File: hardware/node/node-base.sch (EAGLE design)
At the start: 43 parts, among them U1 INA322_DGK_8, U2 LMV551_DBV_5, X1 BU-SMA-V

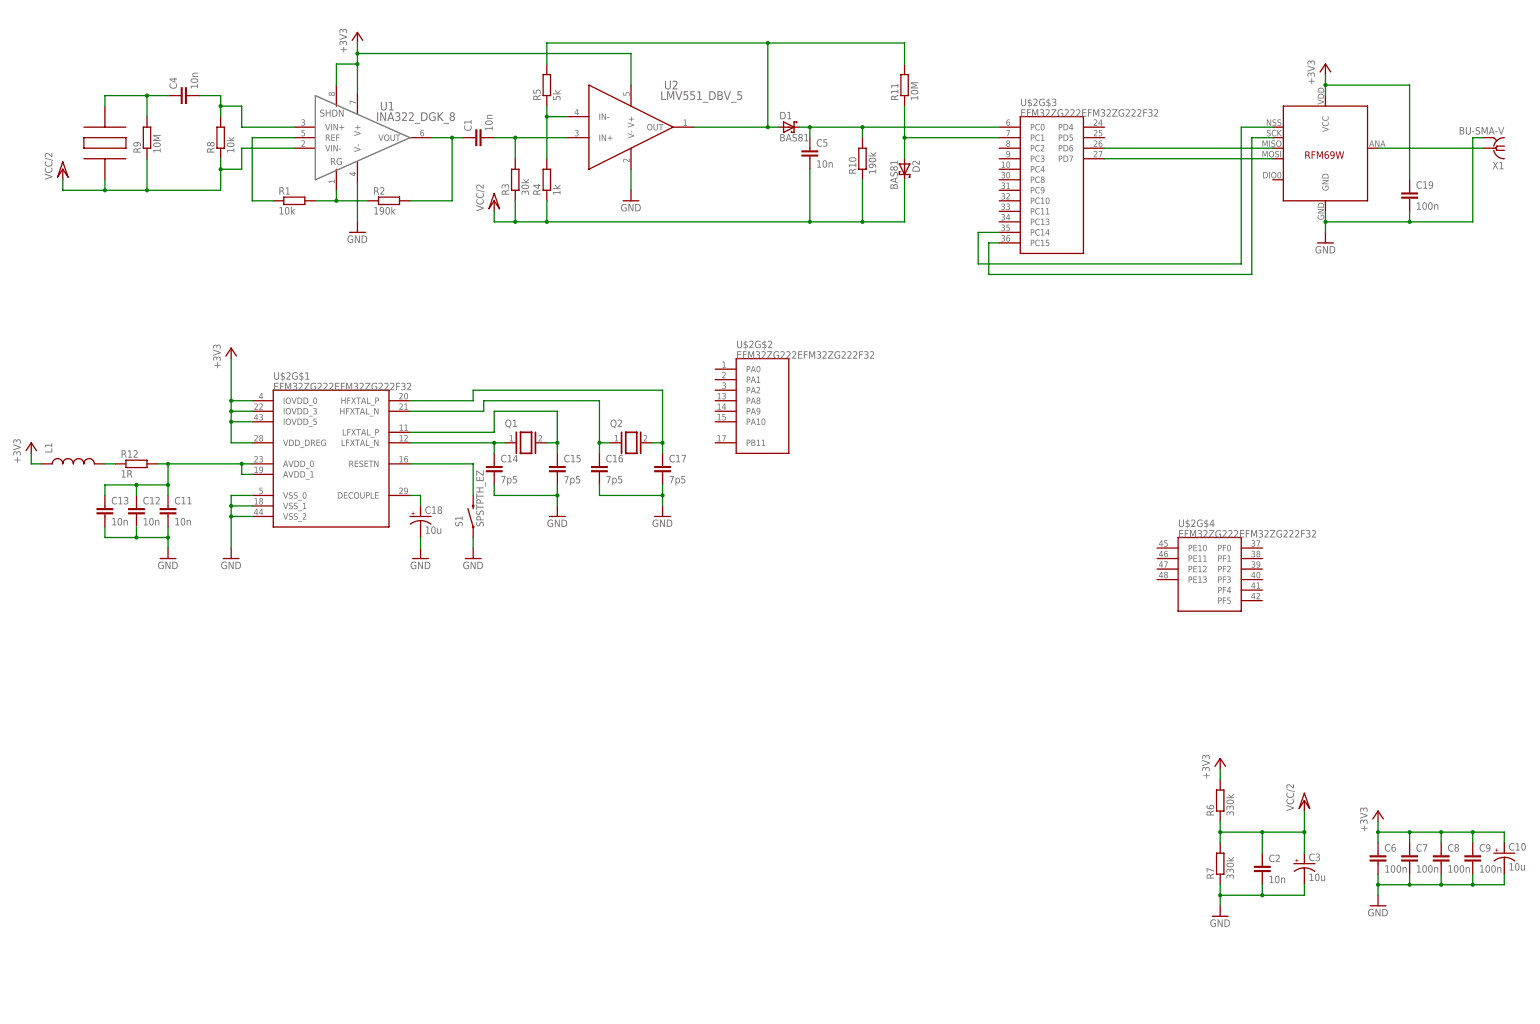
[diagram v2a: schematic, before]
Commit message: NODE: Added sensors, power control
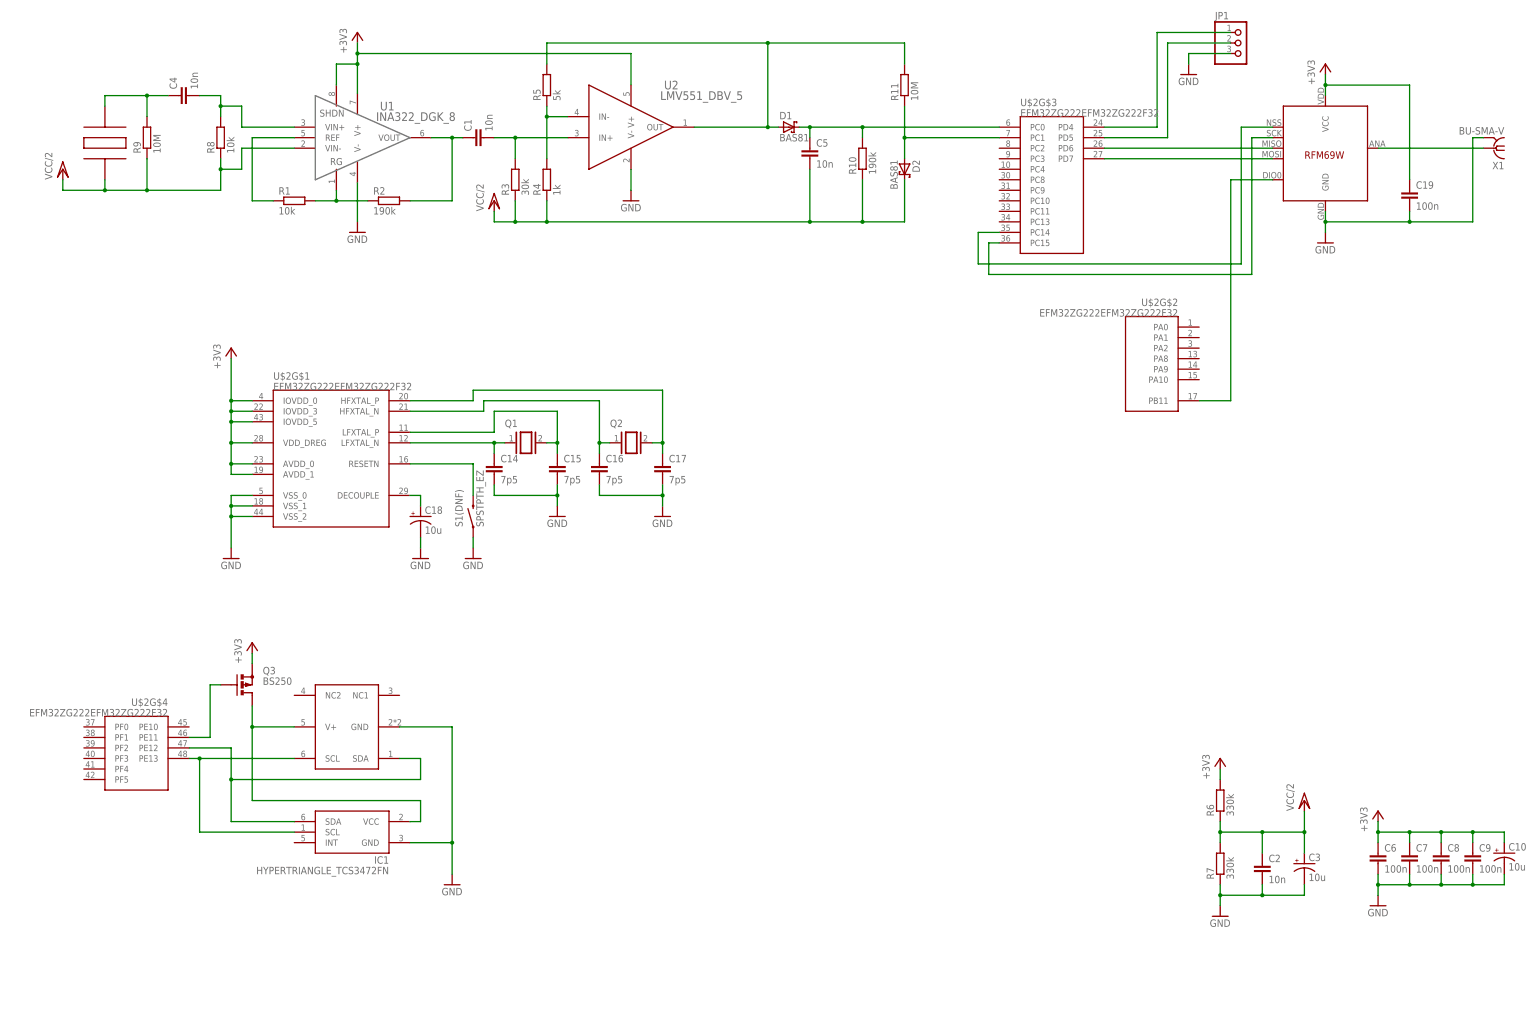
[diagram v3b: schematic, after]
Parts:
- removed C11, C12, C13: 10n, SparkFun-Capacitors:CAPPTH
- removed L1: (no value), SparkFun-Passives:INDUCTOR0805
- removed R12: 1R, resistor:R-EU_0309/12
- added IC1: HYPERTRIANGLE_TCS3472FN, lightsensor:HYPERTRIANGLE_TCS3472FN
- added JP1: (no value), pinhead:PINHD-1X3
- added Q3: BS250, transistor-small-signal:BS250
- added RADIO: RFM69, Moteino:RFM69
- U$3: value RFM69 -> SHT21; device Moteino:RFM69 -> SHT21:SHT21
- renumbered S1 to S1(DNF)
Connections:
- removed net N$6: L1.2, R12.1
- removed net N$8: C11.1, C12.1, C13.1, R12.2, U$2G$1.AVDD_0, U$2G$1.AVDD_1
- new net CON_EXTSENSOR: JP1.1, U$2G$3.PD4
- new net N$21: RADIO.DIO0, U$2G$2.PB11
- new net N$24: IC1.VCC, Q3.D, U$3.V+
- new net N$25: IC1.SCL, U$2G$4.PE13, U$3.SCL
- new net N$26: JP1.2, U$2G$3.PD5
- new net N$27: IC1.SDA, U$2G$4.PE12, U$3.SDA
- new net N$28: Q3.G, U$2G$4.PE11
- net +3V3: now also Q3.S, RADIO.VCC, U$2G$1.AVDD_0, U$2G$1.AVDD_1; no longer L1.1, U$3.VCC
- net GND: now also IC1.GND, JP1.3, RADIO.GND; no longer C11.2, C12.2, C13.2
- net N$13: now also RADIO.MISO; no longer U$3.MISO
- net N$15: now also RADIO.MOSI; no longer U$3.MOSI
- net N$19: now also RADIO.SEL; no longer U$3.SEL
- net N$20: now also RADIO.SCK; no longer U$3.SCK
- net N$22: now also RADIO.ANT; no longer U$3.ANT
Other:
- moved on the sheet: U$2G$2, U$2G$4

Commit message: NODEHW: Finished first schematic draft
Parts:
- added C11: 10n, SparkFun-Capacitors:CAPPTH
- added CON_EXTSENSOR: (no value), pinhead:PINHD-1X3
- added LED1: RED, led:LED3MM
- added LED2: YELLOW, led:LED3MM
- added LED3: GREEN, led:LED3MM
- added R12: 1M, resistor:R-EU_0309/12
- added R13, R14, R15: 220, resistor:R-EU_0309/12
- added S1(DNF)1: SPSTPTH_EZ, SparkFun-Electromechanical:SPSTPTH_EZ
- JP1: device pinhead:PINHD-1X3 -> pinhead:PINHD-1X6
- Q1: value (none) -> 32.768kHz
- Q2: value (none) -> 24MHz
- U$2: value EFM32ZG222EFM32ZG222F32 -> EFM32ZG222F32; device FullyCustom:EFM32ZG222EFM32ZG222F32 -> FullyCustom:EFM32ZG222F32
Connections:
- net N$1 renamed RGLINE
- net N$10 renamed INSTR_FILTERED
- net N$11 renamed OPAMP_VGND
- net N$13 renamed RADIO_MISO
- net N$14 renamed LFXTAL_P
- net N$15 renamed RADIO_MOSI
- net N$16 renamed LFXTAL_N
- net N$17 renamed XTALP
- net N$18 renamed XTALN
- net N$19 renamed RADIO_CS
- net N$2 renamed OPAMP_OUT
- net N$20 renamed RADIO_SCK
- net N$21 renamed RADIO_INT
- net N$22 renamed RADIO_ANT
- net N$23 renamed DECOUPLE
- net N$24 renamed EXT_PWRLINE
- net N$25 renamed SCL
- net N$27 renamed SDA
- net N$28 renamed EXT_PWRUP
- net N$3 renamed DETECT_REF
- net N$4 renamed PIEZO_FILTERED
- net N$5 renamed PIEZO_OUT
- net N$7 renamed REFLINE
- net N$9 renamed INSTR_OUT
- removed net CON_EXTSENSOR: JP1.1, U$2G$3.PD4
- removed net N$12: S1(DNF).2, U$2G$1.RESETN
- removed net N$26: JP1.2, U$2G$3.PD5
- new net EXTSENS_RX: CON_EXTSENSOR.2, U$2G$3.PD5
- new net EXTSENS_TX: CON_EXTSENSOR.1, U$2G$3.PD4
- new net LED_GREEN: LED3.A, U$2G$4.PF3
- new net LED_RED: LED1.A, U$2G$4.PF5
- new net LED_SWITCH: C11.1, R12.1, S1(DNF)1.2, U$2G$4.PE10
- new net LED_YELLOW: LED2.A, U$2G$4.PF4
- new net N$10: LED2.C, R14.2
- new net N$11: LED3.C, R15.2
- new net N$9: LED1.C, R13.2
- new net RESET: JP1.5, S1(DNF).2, U$2G$1.RESETN
- new net SWCLK: JP1.2, U$2G$4.PF0
- new net SWDIO: JP1.4, U$2G$4.PF1
- new net SWO: JP1.6, U$2G$4.PF2
- net +3V3: now also JP1.1, R12.2
- net GND: now also C11.2, CON_EXTSENSOR.3, R13.1, R14.1, R15.1, S1(DNF)1.1
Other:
- note added: "MCU Power & Debug"
- note added: "Sensors & Radio"

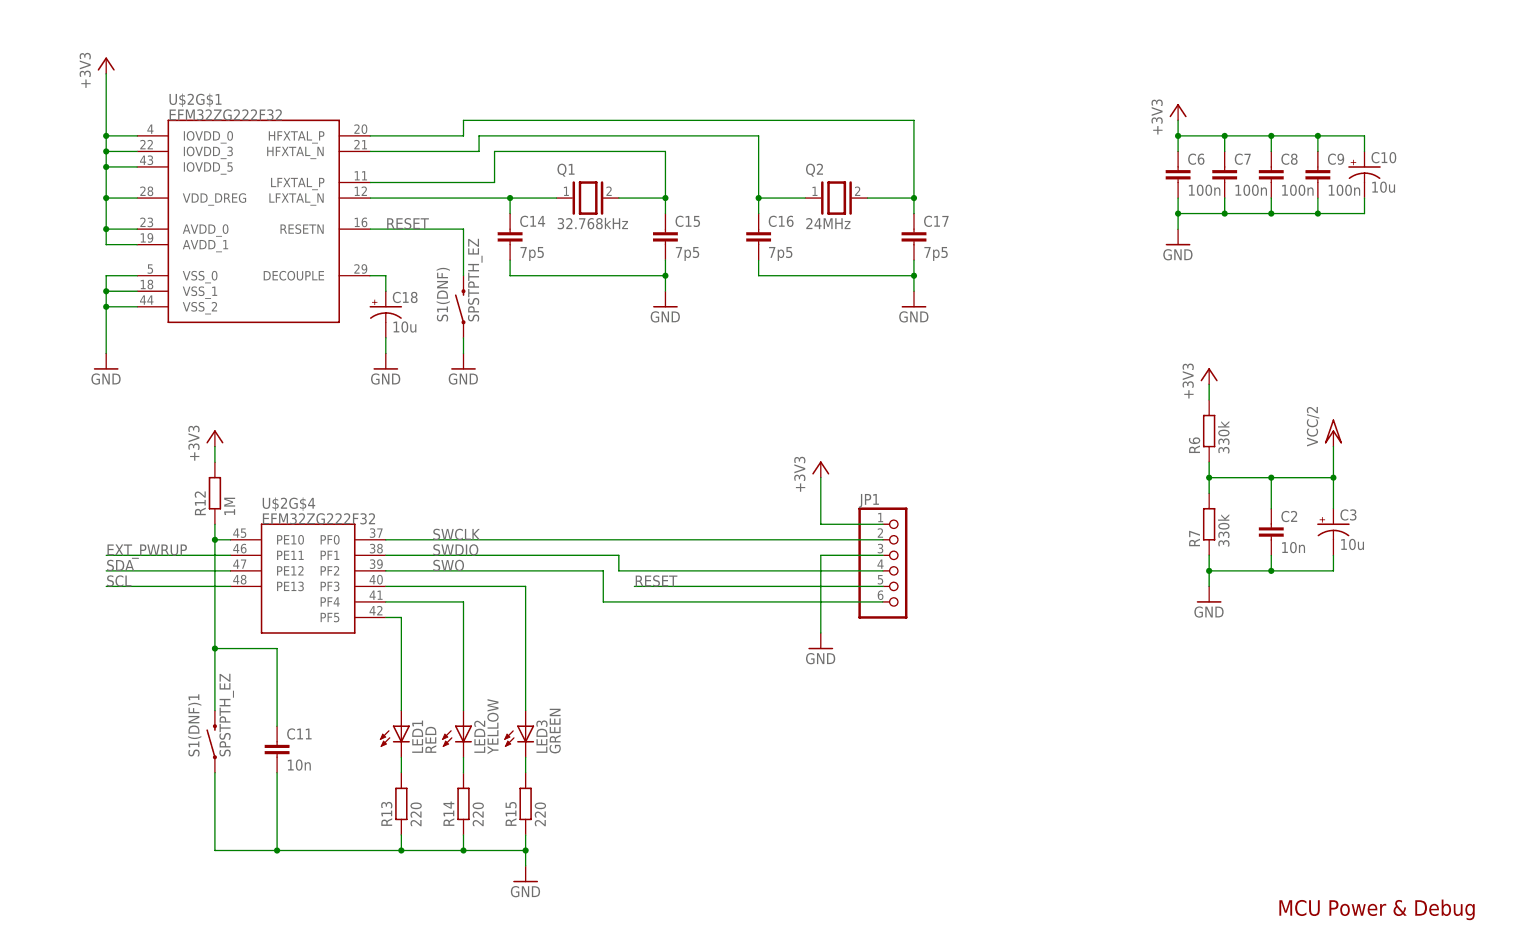
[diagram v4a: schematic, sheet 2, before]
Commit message: NODEHW: Schematic basically finished
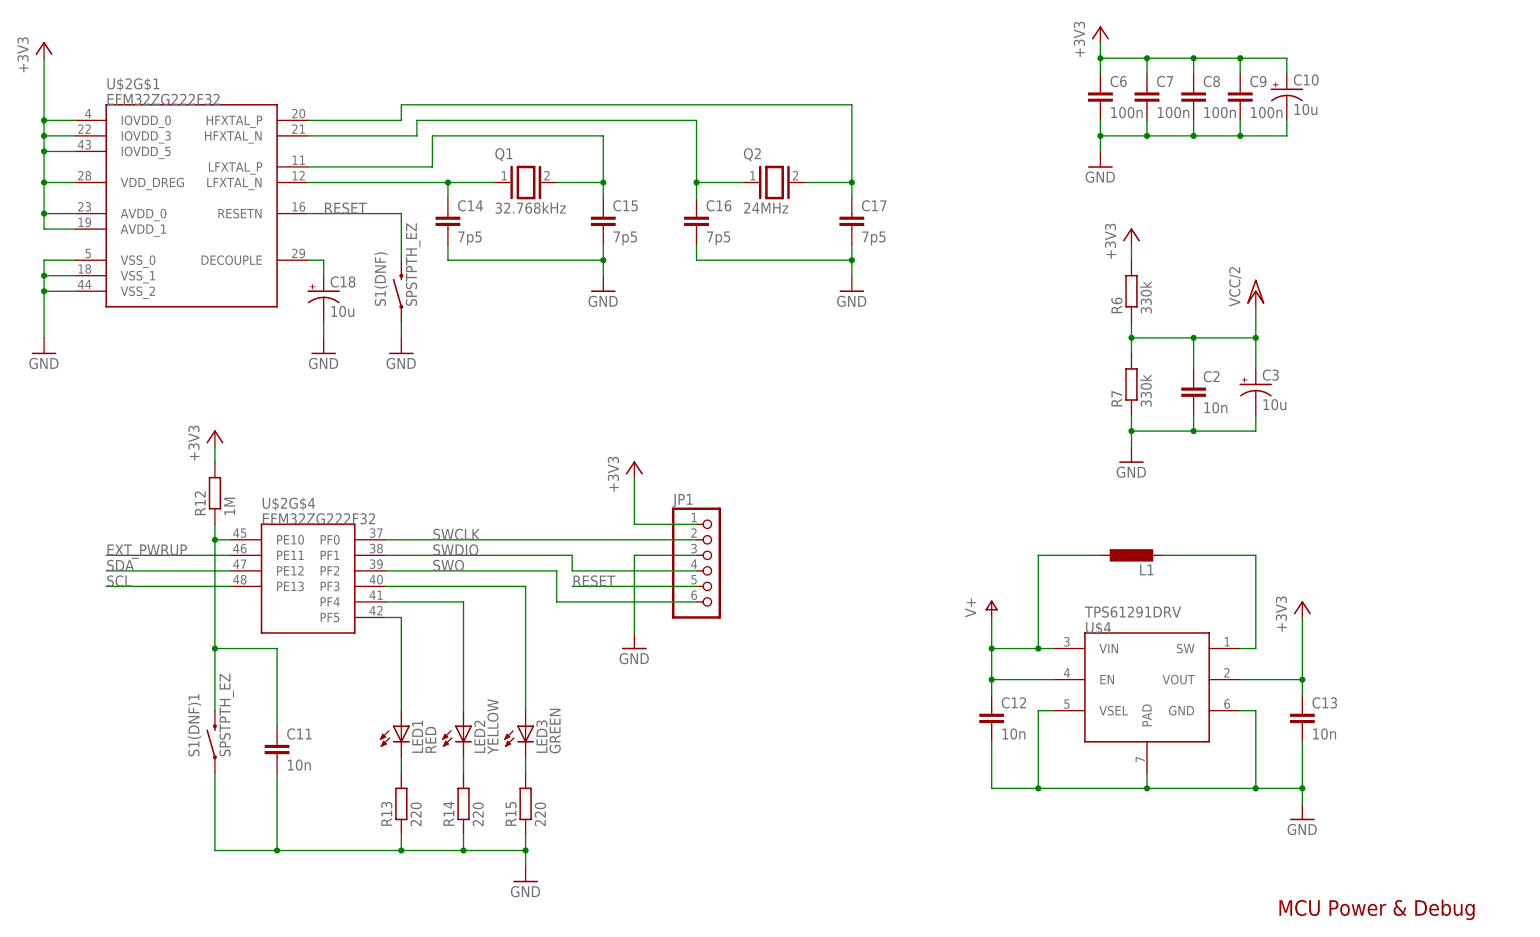
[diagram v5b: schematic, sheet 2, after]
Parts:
- added C12, C13: 10n, SparkFun-Capacitors:CAPPTH
- added L1: (no value), resistor:L-EU0207/10
- added U$4: TPS61291DRV, FullyCustom:TPS61291DRV
- R1, R10, R11, R12, R13, R14, R15, R2, R3, R4, R5, R8, R9: device resistor:R-EU_0309/12 -> resistor:R-EU_0204/7
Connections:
- new net N$4: L1.2, U$4.SW
- new net V+: C12.1, L1.1, U$4.EN, U$4.VIN
- net +3V3: now also C13.1, U$4.VOUT
- net EXT_PWRUP: now also U$2G$3.PC8
- net GND: now also C12.2, C13.2, U$4.GND, U$4.PAD, U$4.VSEL
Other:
- note added: "CHECK PC8 doesn't do anything else"
- moved on the sheet: C10, C14, C15, C16, C17, C18, C2, C3, C6, C7, C8, C9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
